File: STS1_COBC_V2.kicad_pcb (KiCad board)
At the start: 4 copper layers, 81 x 85 mm, 222 parts, among them IC2 STWD100PYW83F, IC3 STM32F411RET6TR, J1 UHF, J12 Conn_01x01_Male, J13 Conn_01x01_Male, J16 Conn_ARM_JTAG_SWD_10, J17 Conn_01x03_Male, J3 Conn_01x01_Male, J4 Conn_01x01_Male, J5 Conn_01x03_Male, J6 Conn_01x01_Male, J7 Conn_01x01_Male, J8 Conn_01x01_Male, J9 Conn_01x01_Male, Q1 SQ2318, Q2 BSS123, U1 coordinate_system, U10 TQP3M9036, U11 QPC1022, U12 FPF2701, U13 TQP7M9106, U14 MC14541BD, U15 MC74HC4538ADG, U2 LP2985-1.8, U3 MCP1725-3302E_MC, U4 74LVC2G74, U5 TYKTBCSANF-26.000000, U6 MP28167GQ, U7 NL17SV04XV5T2G, U8 Si4463, U9 LFCG-490+, Y1 Crystal_GND24

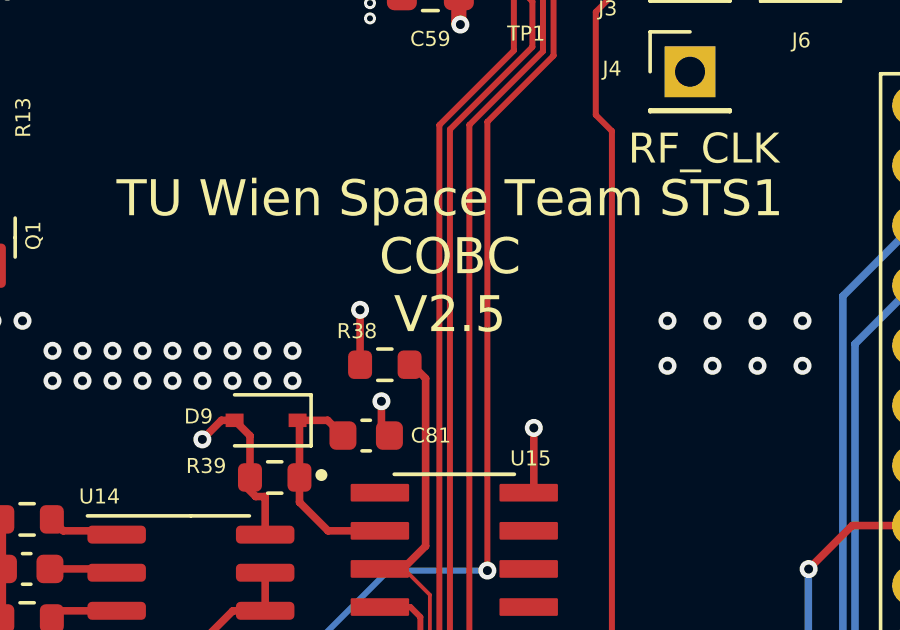
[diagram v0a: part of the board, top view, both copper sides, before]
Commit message: Change version on schematics/pcb to v2.6
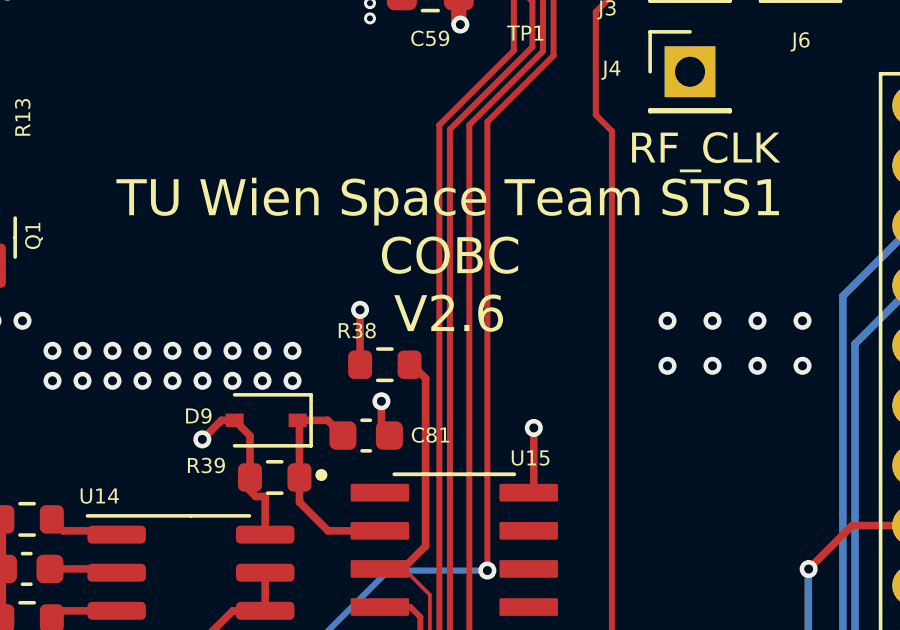
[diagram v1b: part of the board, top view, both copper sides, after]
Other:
- board text added: "TU Wien Space Team STS1 COBC V2.6"
- board text removed: "TU Wien Space Team STS1 COBC V2.5"
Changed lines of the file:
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@@
   (gr_line (start 120.6 126.8) (end 192.6 126.8) (layer "Edge.Cuts") (width 0.15))
   (gr_line (start 116.1 46.3) (end 116.1 122.3) (layer "Edge.Cuts") (width 0.15))
-  (gr_text "TU Wien Space Team STS1\nCOBC\nV2.5" (at 177.187 69.3315) (layer "F.SilkS")
+  (gr_text "TU Wien Space Team STS1\nCOBC\nV2.6" (at 177.187 69.3315) (layer "F.SilkS")
     (effects (font (size 1.2 1.2) (thickness 0.2)))
   )

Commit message: Rotate coordinate system (x,y,z)->(y,-x,z)
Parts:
- moved U1 0.63 mm to (123.3, 55.1), turned to 90 degrees
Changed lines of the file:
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@@
   )
   (footprint "STS_connector:Coordinates" (layer "F.Cu")
-    (at 122.8 55.4255)
+    (at 123.339 55.1075 90)
     (property "Sheetfile" "STS1_COBC_V2.kicad_sch")
     (property "Sheetname" "")
     (attr through_hole)
-    (fp_text reference "U1" (at 0 0) (layer "F.SilkS") hide
+    (fp_text reference "U1" (at 0 0 90) (layer "F.SilkS") hide
       (effects (font (size 0.5 0.5) (thickness 0.1)))
     )
-    (fp_text value "coordinate_system" (at 0.75 0) (layer "F.SilkS") hide
+    (fp_text value "coordinate_system" (at 0.75 0 90) (layer "F.SilkS") hide
       (effects (font (size 1.524 1.524) (thickness 0.3)))
     )

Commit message: Modify resetdog
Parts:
- D10, D9: footprint Diode_SMD:D_SOD-323 -> Diode_SMD:D_SOD-123F
- moved R40 1.78 mm to (160.6, 87.9)
- moved D10 1.70 mm to (161.5, 85.0)
- moved R39 1.53 mm to (169.9, 77.1)
- moved D9 0.69 mm to (170.5, 75.1)
- moved C83 0.11 mm to (158.2, 83.6)
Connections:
- U14 pad 9: AGND -> +3V3
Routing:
- net +3V3: track 143.3 -> 153.0 mm
- net AGND: track 188.3 -> 186.8 mm
- net /WDT_CLR: track 45.1 -> 46.6 mm
- net /RDT_CLR: track 32.0 -> 33.4 mm
- net Net-(C81-Pad1): track 7.66 -> 8.88 mm
